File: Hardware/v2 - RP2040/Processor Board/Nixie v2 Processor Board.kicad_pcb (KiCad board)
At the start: 2 copper layers, 100 x 100 mm, 90 parts, among them J1 Conn_02x02_2.54mm, J2 USB_C_Receptacle_USB2.0, J3 Conn_01x03_2.54mm, J4 Conn_01x03_2.54mm, Q1 PZTA92, Q3 MMBTA42, SW1 SW_Push, SW2 SW_Push, SW3 SW_DIP_x10, SW4 SW_Push, U10 W25Q128JVP, U11 L80-M39, U12 DS3231MZ, U13 TC2185-3.3VCTTR, U14 MCP23017_SS, U3 TPS62933, U4 К155ИД1, U5 К155ИД1, U6 К155ИД1, U7 MCP23017_ML, U7 К155ИД1, U8 AP22913, U9 RP2040

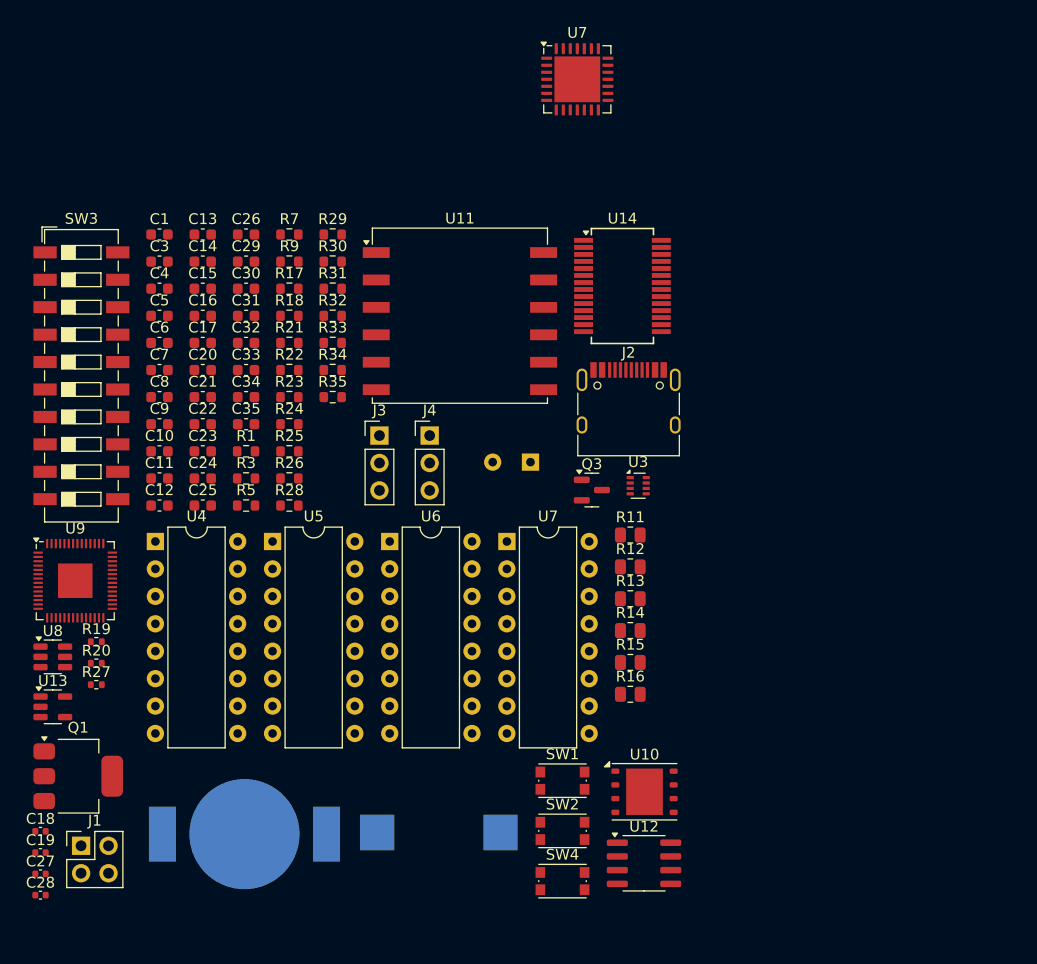
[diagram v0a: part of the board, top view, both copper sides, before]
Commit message: seperated the processor and nixie boards
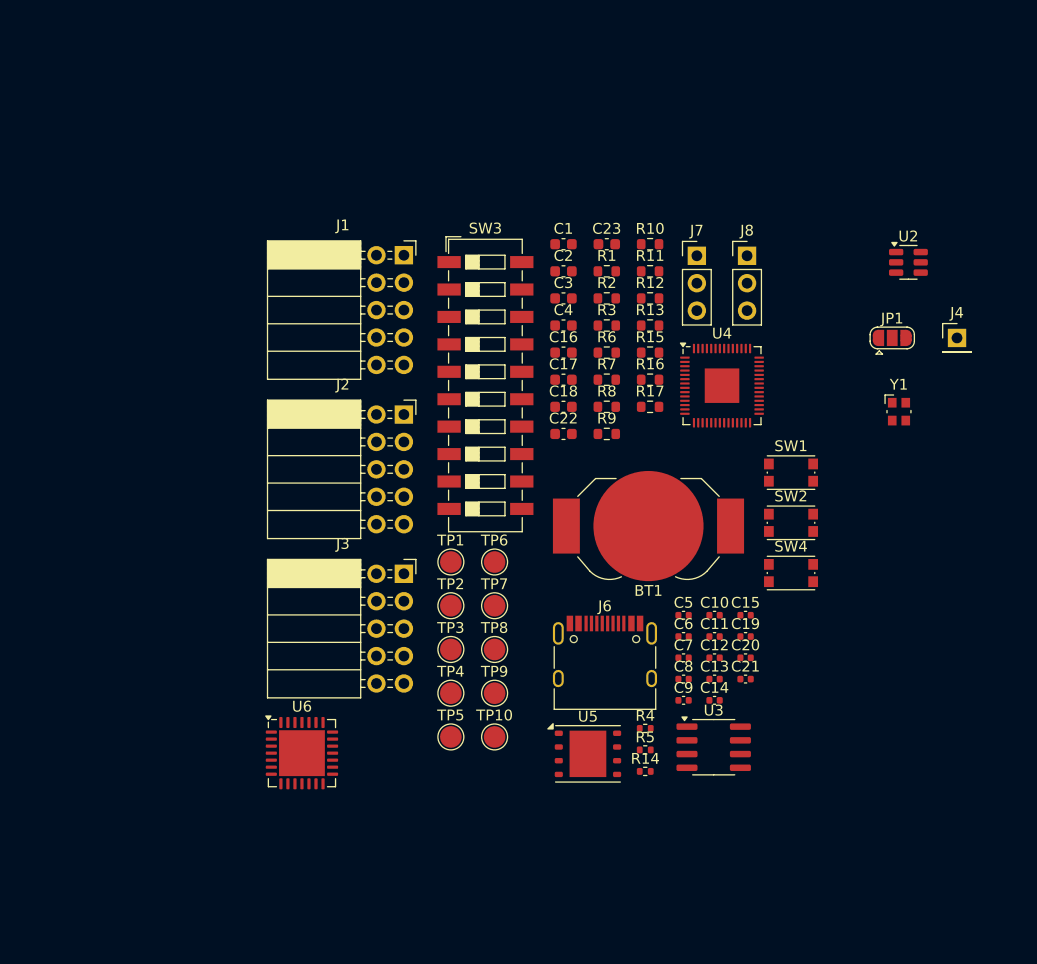
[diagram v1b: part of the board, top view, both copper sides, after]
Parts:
- removed C24, C25, C29, C33, C35: 100n, Capacitor_SMD:C_0603_1608Metric
- removed C26: 10u, Capacitor_SMD:C_0603_1608Metric
- removed C27, C28: 8p, Capacitor_SMD:C_0402_1005Metric
- removed C30, C31, C34: 1u, Capacitor_SMD:C_0603_1608Metric
- removed C32: 10n, Capacitor_SMD:C_0603_1608Metric
- removed L1: 7.8u, Inductor_SMD:L_Vishay_IHLP-5050
- removed Q1: PZTA92, Package_TO_SOT_SMD:SOT-223-3_TabPin2
- removed Q3: MMBTA42, Package_TO_SOT_SMD:SOT-23
- removed R18, R23, R24, R26, R30, R31, R32, R35: 10k, Resistor_SMD:R_0603_1608Metric
- removed R19, R20: 27.4, Resistor_SMD:R_0402_1005Metric
- removed R21, R22: 5.1k, Resistor_SMD:R_0603_1608Metric
- removed R25: 1k, Resistor_SMD:R_0603_1608Metric
- removed R27: 1k, Resistor_SMD:R_0402_1005Metric
- removed R28, R29: 2.2k, Resistor_SMD:R_0603_1608Metric
- removed R33: R_Photo, Resistor_SMD:R_0603_1608Metric
- removed R34: 150, Resistor_SMD:R_0603_1608Metric
- removed U10: W25Q128JVP, Package_SON:WSON-8-1EP_6x5mm_P1.27mm_EP3.4x4.3mm
- removed U11: L80-M39, RF_GPS:Quectel_L80-R
- removed U12: DS3231MZ, Package_SO:SOIC-8_3.9x4.9mm_P1.27mm
- removed U13: TC2185-3.3VCTTR, Package_TO_SOT_SMD:SOT-23-5
- removed U14: MCP23017_SS, Package_SO:SSOP-28_5.3x10.2mm_P0.65mm
- removed U7: MCP23017_ML, Package_DFN_QFN:QFN-28-1EP_6x6mm_P0.65mm_EP4.25x4.25mm
- removed U7: К155ИД1, Package_DIP:DIP-16_W7.62mm
- removed U8: AP22913, Package_TO_SOT_SMD:SOT-23-6
- removed U9: RP2040, Package_DFN_QFN:QFN-56-1EP_7x7mm_P0.4mm_EP3.2x3.2mm
- added J6: USB_C_Receptacle_USB2.0, Connector_USB:USB_C_Receptacle_HRO_TYPE-C-31-M-12, F.Cu at (-36.6, 43.5)
- added J7: Conn_01x03_2.54mm, Connector_PinHeader_2.54mm:PinHeader_1x03_P2.54mm_Vertical, F.Cu at (-28.1, 5.39)
- added J8: Conn_01x03_2.54mm, Connector_PinHeader_2.54mm:PinHeader_1x03_P2.54mm_Vertical, F.Cu at (-23.4, 5.39)
- added JP1: SolderJumper_3_Open, Jumper:SolderJumper-3_P1.3mm_Open_RoundedPad1.0x1.5mm, F.Cu at (-10.0, 13.0)
- added R10: 2.2k, Resistor_SMD:R_0603_1608Metric, F.Cu at (-32.4, 4.32)
- added R2: 169k, Resistor_SMD:R_0603_1608Metric, F.Cu at (-36.4, 9.34)
- added R4: 27.4, Resistor_SMD:R_0402_1005Metric, F.Cu at (-32.9, 49.2)
- added R6: 5.1k, Resistor_SMD:R_0603_1608Metric, F.Cu at (-36.4, 14.4)
- added R8: 10k, Resistor_SMD:R_0603_1608Metric, F.Cu at (-36.4, 19.4)
- added TP1: TestPoint, TestPoint:TestPoint_Pad_D2.0mm, F.Cu at (-50.9, 33.8)
- added TP10: TestPoint, TestPoint:TestPoint_Pad_D2.0mm, F.Cu at (-46.8, 50.0)
- added TP2: TestPoint, TestPoint:TestPoint_Pad_D2.0mm, F.Cu at (-50.9, 37.8)
- added TP3: TestPoint, TestPoint:TestPoint_Pad_D2.0mm, F.Cu at (-50.9, 41.9)
- added TP4: TestPoint, TestPoint:TestPoint_Pad_D2.0mm, F.Cu at (-50.9, 45.9)
- added TP5: TestPoint, TestPoint:TestPoint_Pad_D2.0mm, F.Cu at (-50.9, 50.0)
- added TP6: TestPoint, TestPoint:TestPoint_Pad_D2.0mm, F.Cu at (-46.8, 33.8)
- added TP7: TestPoint, TestPoint:TestPoint_Pad_D2.0mm, F.Cu at (-46.8, 37.8)
- added TP8: TestPoint, TestPoint:TestPoint_Pad_D2.0mm, F.Cu at (-46.8, 41.9)
- added TP9: TestPoint, TestPoint:TestPoint_Pad_D2.0mm, F.Cu at (-46.8, 45.9)
- added U2: AP22913, Package_TO_SOT_SMD:SOT-23-6, F.Cu at (-8.50, 6.00)
- added Y1: 12MHz, Crystal:Crystal_SMD_Abracon_ABM10-4Pin_2.5x2.0mm, F.Cu at (-9.38, 19.8)
- BT1: moved to F.Cu
- C1: value 100u -> 10u
- C10, C11, C12, C13, C5, C9: footprint Capacitor_SMD:C_0603_1608Metric -> Capacitor_SMD:C_0402_1005Metric
- C14, C15: value 100n -> 1u; footprint Capacitor_SMD:C_0603_1608Metric -> Capacitor_SMD:C_0402_1005Metric
- C18: value 1u -> 100n; footprint Capacitor_SMD:C_0402_1005Metric -> Capacitor_SMD:C_0603_1608Metric
- C2: value 4.7u -> 22u; footprint Capacitor_THT:CP_Radial_D8.0mm_P3.50mm -> Capacitor_SMD:C_0603_1608Metric; moved to F.Cu
- C20, C21: value 100n -> 8p; footprint Capacitor_SMD:C_0603_1608Metric -> Capacitor_SMD:C_0402_1005Metric
- C22, C23: value 1u -> 100n
- C3: value 100n -> 1u
- C4: value 10u -> 1u
- C6: value 82p -> 100n; footprint Capacitor_SMD:C_0603_1608Metric -> Capacitor_SMD:C_0402_1005Metric
- C7: value 33n -> 100n; footprint Capacitor_SMD:C_0603_1608Metric -> Capacitor_SMD:C_0402_1005Metric
- C8: value 47u -> 100n; footprint Capacitor_SMD:C_0603_1608Metric -> Capacitor_SMD:C_0402_1005Metric
- J1: value Conn_02x02_2.54mm -> Conn_01x10_Socket; footprint Connector_PinHeader_2.54mm:PinHeader_2x02_P2.54mm_Vertical -> Connector_PinSocket_2.54mm:PinSocket_2x05_P2.54mm_Horizontal
- J2: value USB_C_Receptacle_USB2.0 -> Conn_01x10_Socket; footprint Connector_USB:USB_C_Receptacle_HRO_TYPE-C-31-M-12 -> Connector_PinSocket_2.54mm:PinSocket_2x05_P2.54mm_Horizontal
- J3: value Conn_01x03_2.54mm -> Conn_01x10_Socket; footprint Connector_PinHeader_2.54mm:PinHeader_1x03_P2.54mm_Vertical -> Connector_PinSocket_2.54mm:PinSocket_2x05_P2.54mm_Horizontal
- J4: value Conn_01x03_2.54mm -> Conn_01x01_Pin; footprint Connector_PinHeader_2.54mm:PinHeader_1x03_P2.54mm_Vertical -> Connector_PinHeader_2.54mm:PinHeader_1x01_P2.54mm_Vertical
- R1: value 100k -> 523k
- R11, R15, R16: value 22k -> 10k; footprint Resistor_SMD:R_0805_2012Metric -> Resistor_SMD:R_0603_1608Metric
- R12: value 22k -> 1k; footprint Resistor_SMD:R_0805_2012Metric -> Resistor_SMD:R_0603_1608Metric
- R13: value 220k -> 10k; footprint Resistor_SMD:R_0805_2012Metric -> Resistor_SMD:R_0603_1608Metric
- R14: value 220k -> 1k; footprint Resistor_SMD:R_0805_2012Metric -> Resistor_SMD:R_0402_1005Metric
- R17: value 30.9 -> 10k
- R3: value 100k -> 499k
- R5: value 100k -> 27.4; footprint Resistor_SMD:R_0603_1608Metric -> Resistor_SMD:R_0402_1005Metric
- R7: value 10k -> 5.1k
- R9: value 10k -> 2.2k
- U3: value TPS62933 -> DS3231MZ; footprint Package_TO_SOT_SMD:SOT-583-8 -> Package_SO:SOIC-8_3.9x4.9mm_P1.27mm
- U4: value К155ИД1 -> RP2040; footprint Package_DIP:DIP-16_W7.62mm -> Package_DFN_QFN:QFN-56-1EP_7x7mm_P0.4mm_EP3.2x3.2mm
- U5: value К155ИД1 -> W25Q128JVP; footprint Package_DIP:DIP-16_W7.62mm -> Package_SON:WSON-8-1EP_6x5mm_P1.27mm_EP3.4x4.3mm
- U6: value К155ИД1 -> MCP23017_ML; footprint Package_DIP:DIP-16_W7.62mm -> Package_DFN_QFN:QFN-28-1EP_6x6mm_P0.65mm_EP4.25x4.25mm
- moved C19 68.3 mm to (-23.6, 40.6)
- moved C13 62.8 mm to (-26.5, 44.6)
- moved C14 62.4 mm to (-26.5, 46.6)
- moved C18 62.4 mm to (-40.4, 19.4)
- moved J1 62.3 mm to (-55.2, 5.34)
- moved C15 58.7 mm to (-23.6, 38.7)
- moved C20 56.9 mm to (-23.6, 42.6)
- moved C21 56.6 mm to (-23.6, 44.6)
- moved C5 55.9 mm to (-29.3, 38.7)
- moved C6 55.6 mm to (-29.3, 40.6)
- moved C7 55.4 mm to (-29.3, 42.6)
- moved C8 55.1 mm to (-29.3, 44.6)
- moved C9 54.9 mm to (-29.3, 46.6)
- moved U4 54.4 mm to (-25.8, 17.4)
- moved C10 53.6 mm to (-26.5, 38.7)
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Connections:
- C10 pad 1: +1V1 -> +3.3V
- C14 pad 1: +3.3V -> +1V1
- C16 pad 1: +3.3V -> Net-(U4-RUN)
- C17 pad 1: +3.3V -> +3V3
- C18 pad 1: +1V1 -> Net-(C18-Pad1)
- C19 pad 1: +3.3V -> Net-(BT1-+)
- C2 pad 1: /170V_1 -> +3.3V
- C20 pad 1: Net-(U9-RUN) -> GND
- C20 pad 2: GND -> Net-(U4-XIN)
- C21 pad 1: Net-(C21-Pad1) -> GND
- C21 pad 2: GND -> Net-(C21-Pad2)
- C23 pad 1: Net-(U11-VCC) -> Net-(U6-GPA2)
- C3 pad 1: Net-(U3-BST) -> Net-(JP1-C)
- C3 pad 2: Net-(U3-SW) -> GND
- C4 pad 1: VBUS -> Net-(U2-OUT)
- C5 pad 1: VBUS -> +1V1
- C6 pad 1: +3.3V -> +1V1
- C6 pad 2: Net-(U3-FB) -> GND
- C7 pad 1: Net-(U3-SS) -> +3.3V
- C9 pad 1: +1V1 -> +3.3V
- J1 pad 2: Net-(J1-Pin_2) -> /Hours_Tens_A
- J1 pad 3: GND -> /Hours_Tens_D
- J1 pad 4: Net-(J1-Pin_4) -> /Hours_Tens_B
- J3 pad 1: GND -> VBUS
- J3 pad 2: /UART0 RX -> VBUS
- J3 pad 3: /UART0 TX -> +3.3V
- J4 pad 1: Net-(J4-Pin_1) -> /UART1_TX
- R1 pad 1: /170V_1 -> Net-(U1-FB)
- R1 pad 2: Net-(Q1-B) -> +3.3V
- R11 pad 1: /ANODE_1 -> Net-(C18-Pad1)
- R11 pad 2: Net-(N1-Anode) -> +3.3V
- R12 pad 1: /ANODE_1 -> Net-(U4-QSPI_SS)
- R12 pad 2: Net-(N2-Anode) -> Net-(C18-Pad1)
- R13 pad 1: /ANODE_1 -> +3V3
- R13 pad 2: Net-(J1-Pin_2) -> /RTC_Interrupt
- R14 pad 1: /ANODE_1 -> Net-(U4-XOUT)
- R14 pad 2: Net-(J1-Pin_4) -> Net-(C21-Pad2)
- R15 pad 1: /ANODE_1 -> +3V3
- R15 pad 2: Net-(N3-Anode) -> Net-(U6-~{RESET})
- R16 pad 1: /ANODE_1 -> +3V3
- R16 pad 2: Net-(N4-Anode) -> /Settings_Interrupt
- R17 pad 1: Net-(U3-FB) -> +3V3
- R17 pad 2: +3.3V -> Net-(U6-INTB)
- R3 pad 1: Net-(Q1-B) -> Net-(U1-PG)
- R3 pad 2: Net-(R3-Pad2) -> +3.3V
- R5 pad 1: Net-(R3-Pad2) -> Net-(U4-USB_DP)
- R7 pad 1: /Dimming -> GND
- R9 pad 1: /Dimming -> +3V3
- R9 pad 2: GND -> /I2C1_SCL
- SW1 pad 2: Net-(U9-RUN) -> Net-(U4-RUN)
- SW2 pad 2: Net-(C21-Pad1) -> Net-(C18-Pad1)
- SW3 pad 1: Net-(U7-GPB0) -> Net-(U6-GPB0)
- SW3 pad 10: Net-(U7-GPA1) -> Net-(U6-GPA1)
- SW3 pad 2: Net-(U7-GPB1) -> Net-(U6-GPB1)
- SW3 pad 3: Net-(U7-GPB2) -> Net-(U6-GPB2)
- SW3 pad 4: Net-(U7-GPB3) -> Net-(U6-GPB3)
- SW3 pad 5: Net-(U7-GPB4) -> Net-(U6-GPB4)
- SW3 pad 6: Net-(U7-GPB5) -> Net-(U6-GPB5)
- SW3 pad 7: Net-(U7-GPB6) -> Net-(U6-GPB6)
- SW3 pad 8: Net-(U7-GPB7) -> Net-(U6-GPB7)
- SW3 pad 9: Net-(U7-GPA0) -> Net-(U6-GPA0)
- SW4 pad 1: Net-(U7-GPA2) -> Net-(U6-GPA2)
- U3 pad 2: unconnected-(U3-EN-Pad2) -> +3V3
- U3 pad 3: VBUS -> /RTC_Interrupt
- U3 pad 4: GND -> +3V3
- U3 pad 5: Net-(U3-SW) -> GND
- U3 pad 6: Net-(U3-BST) -> Net-(BT1-+)
- U3 pad 7: Net-(U3-SS) -> /I2C1_SDA
- U3 pad 8: Net-(U3-FB) -> /I2C1_SCL
- U4 pad 1: Net-(U4-8) -> +3.3V
- U4 pad 10: Net-(U4-7) -> +3.3V
- U4 pad 11: Net-(U4-6) -> /Hours_Tens_B
- U4 pad 12: GND -> /Hours_Tens_C
- U4 pad 13: Net-(U4-4) -> /Hours_Ones_A
- U4 pad 14: Net-(U4-5) -> /Hours_Ones_D
- U4 pad 15: Net-(U4-1) -> /Hours_Ones_B
- U4 pad 16: Net-(N1-0) -> /Hours_Ones_C
- U4 pad 2: Net-(U4-9) -> /UART0 TX
- U4 pad 3: /Hours_Tens_A -> /UART0 RX
- U4 pad 4: /Hours_Tens_D -> /I2C1_SDA
- U4 pad 5: VBUS -> /I2C1_SCL
- U4 pad 6: /Hours_Tens_B -> /UART1_TX
- U4 pad 7: /Hours_Tens_C -> /UART1_RX
- U4 pad 8: Net-(U4-2) -> /Hours_Tens_A
- U4 pad 9: Net-(U4-3) -> /Hours_Tens_D
- U5 pad 1: Net-(U5-8) -> Net-(U4-QSPI_SS)
- U5 pad 2: Net-(U5-9) -> Net-(U4-QSPI_SD1)
- U5 pad 3: /Hours_Ones_A -> Net-(U4-QSPI_SD2)
- U5 pad 4: /Hours_Ones_D -> GND
- U5 pad 5: VBUS -> Net-(U4-QSPI_SD0)
- U5 pad 6: /Hours_Ones_B -> Net-(U4-QSPI_SCLK)
- U5 pad 7: /Hours_Ones_C -> Net-(U4-QSPI_SD3)
- U5 pad 8: Net-(U5-2) -> +3V3
- U5 pad 9: Net-(U5-3) -> GND
- U6 pad 1: Net-(U6-8) -> Net-(U6-GPB4)
- U6 pad 10: Net-(U6-7) -> unconnected-(U6-NC-Pad10)
- U6 pad 11: Net-(U6-6) -> GND
- U6 pad 13: Net-(U6-4) -> GND
- U6 pad 14: Net-(U6-5) -> Net-(U6-~{RESET})
- U6 pad 15: Net-(U6-1) -> Net-(U6-INTB)
- U6 pad 16: Net-(N3-0) -> /Settings_Interrupt
- U6 pad 2: Net-(U6-9) -> Net-(U6-GPB5)
- U6 pad 3: /Mins_Tens_A -> Net-(U6-GPB6)
- U6 pad 4: /Mins_Tens_D -> Net-(U6-GPB7)
- U6 pad 5: VBUS -> +3V3
- U6 pad 6: /Mins_Tens_B -> GND
- U6 pad 7: /Mins_Tens_C -> unconnected-(U6-NC-Pad7)
- U6 pad 8: Net-(U6-2) -> /I2C1_SCL
- U6 pad 9: Net-(U6-3) -> /I2C1_SDA

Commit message: Started board layout
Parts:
- added H1: MountingHole_Pad, MountingHole:MountingHole_3.2mm_M3_Pad_Via, F.Cu at (105.0, 55.0)
- added H2: MountingHole_Pad, MountingHole:MountingHole_3.2mm_M3_Pad_Via, F.Cu at (195.0, 55.0)
- added H3: MountingHole_Pad, MountingHole:MountingHole_3.2mm_M3_Pad_Via, F.Cu at (105.0, 95.0)
- added H4: MountingHole_Pad, MountingHole:MountingHole_3.2mm_M3_Pad_Via, F.Cu at (195.0, 95.0)
- added J5: AudioJack3_SwitchT, Connector_Audio:Jack_3.5mm_CUI_SJ-3524-SMT_Horizontal, F.Cu at (114.5, 58.7)
- added U1: TPS82084SIL, Nick_Converter_DCDC:MicroSiP 1.33mm, F.Cu at (125.6, 66.4)
- BT1: moved to B.Cu
- C19: footprint Capacitor_SMD:C_0402_1005Metric -> Capacitor_SMD:C_0603_1608Metric
- JP1: footprint Jumper:SolderJumper-3_P1.3mm_Open_RoundedPad1.0x1.5mm -> Jumper:SolderJumper-3_P1.3mm_Open_RoundedPad1.0x1.5mm_NumberLabels
- SW3: footprint Button_Switch_SMD:SW_DIP_SPSTx10_Slide_6.7x26.96mm_W6.73mm_P2.54mm_LowProfile_JPin -> Button_Switch_THT:SW_DIP_SPSTx10_Piano_10.8x26.96mm_W7.62mm_P2.54mm
- moved TP10 243.0 mm to (195.0, 74.0)
- moved TP9 243.0 mm to (195.0, 70.0)
- moved U6 242.6 mm to (177.1, 71.5), turned to 45 degrees
- moved TP6 240.3 mm to (191.0, 68.0)
- moved TP7 240.3 mm to (191.0, 72.0)
- moved TP8 240.3 mm to (191.0, 76.1)
- moved J3 239.9 mm to (178.9, 87.4), turned to 90 degrees
- moved SW3 239.0 mm to (188.4, 54.2), turned to -90 degrees
- moved BT1 229.7 mm to (193.0, 74.0), turned to -90 degrees
- moved U3 193.1 mm to (165.3, 73.3)
- moved U5 186.0 mm to (147.5, 62.5)
- moved SW4 179.4 mm to (159.0, 54.0), turned to 90 degrees
- moved R7 175.0 mm to (132.6, 62.2), turned to 90 degrees
- moved R6 164.6 mm to (121.2, 61.8), turned to 90 degrees
- moved J4 164.1 mm to (-120.5, 128.5)
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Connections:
- C23 pad 1: Net-(U6-GPA2) -> Net-(U6-GPB2)
- J1 pad 1: GND -> /Hours_Ones_B
- J1 pad 10: GND -> /Hours_Tens_A
- J1 pad 2: /Hours_Tens_A -> /Hours_Ones_C
- J1 pad 3: /Hours_Tens_D -> /Hours_Ones_A
- J1 pad 4: /Hours_Tens_B -> /Hours_Ones_D
- J1 pad 5: /Hours_Tens_C -> GND
- J1 pad 6: /Hours_Ones_C -> GND
- J1 pad 7: /Hours_Ones_B -> /Hours_Tens_C
- J1 pad 8: /Hours_Ones_D -> /Hours_Tens_B
- J1 pad 9: /Hours_Ones_A -> /Hours_Tens_D
- J2 pad 1: GND -> /Minutes_Ones_B
- J2 pad 10: GND -> /Minutes_Tens_A
- J2 pad 2: /Minutes_Tens_A -> /Minutes_Ones_C
- J2 pad 3: /Minutes_Tens_D -> /Minutes_Ones_A
- J2 pad 4: /Minutes_Tens_B -> /Minutes_Ones_D
- J2 pad 5: /Minutes_Tens_C -> GND
- J2 pad 6: /Minutes_Ones_C -> GND
- J2 pad 7: /Minutes_Ones_B -> /Minutes_Tens_C
- J2 pad 8: /Minutes_Ones_D -> /Minutes_Tens_B
- J2 pad 9: /Minutes_Ones_A -> /Minutes_Tens_D
- SW3 pad 1: Net-(U6-GPB0) -> GND
- SW3 pad 10: Net-(U6-GPA1) -> GND
- SW3 pad 11: GND -> Net-(U6-GPB1)
- SW3 pad 12: GND -> Net-(U6-GPB0)
- SW3 pad 13: GND -> Net-(U6-GPA7)
- SW3 pad 14: GND -> Net-(U6-GPA6)
- SW3 pad 15: GND -> Net-(U6-GPA5)
- SW3 pad 16: GND -> Net-(U6-GPA4)
- SW3 pad 17: GND -> Net-(U6-GPA3)
- SW3 pad 18: GND -> Net-(U6-GPA2)
- SW3 pad 19: GND -> Net-(U6-GPA1)
- SW3 pad 2: Net-(U6-GPB1) -> GND
- SW3 pad 20: GND -> Net-(U6-GPA0)
- SW3 pad 3: Net-(U6-GPB2) -> GND
- SW3 pad 4: Net-(U6-GPB3) -> GND
- SW3 pad 5: Net-(U6-GPB4) -> GND
- SW3 pad 6: Net-(U6-GPB5) -> GND
- SW3 pad 7: Net-(U6-GPB6) -> GND
- SW3 pad 8: Net-(U6-GPB7) -> GND
- SW3 pad 9: Net-(U6-GPA0) -> GND
- SW4 pad 1: Net-(U6-GPA2) -> Net-(U6-GPB2)
- TP10 pad 1: Net-(U6-GPA7) -> Net-(U6-GPB7)
- TP6 pad 1: Net-(U6-GPA3) -> Net-(U6-GPB3)
- TP7 pad 1: Net-(U6-GPA4) -> Net-(U6-GPB4)
- TP8 pad 1: Net-(U6-GPA5) -> Net-(U6-GPB5)
- TP9 pad 1: Net-(U6-GPA6) -> Net-(U6-GPB6)
- U4 pad 11: /Hours_Tens_B -> /Hours_Ones_A
- U4 pad 12: /Hours_Tens_C -> /Hours_Ones_D
- U4 pad 13: /Hours_Ones_A -> /Hours_Tens_C
- U4 pad 14: /Hours_Ones_D -> /Hours_Tens_B
- U4 pad 15: /Hours_Ones_B -> /Hours_Tens_D
- U4 pad 16: /Hours_Ones_C -> /Hours_Tens_A
- U4 pad 17: /Minutes_Tens_A -> /Minutes_Ones_C
- U4 pad 18: /Minutes_Tens_D -> /Minutes_Ones_B
- U4 pad 27: /Minutes_Tens_B -> /Minutes_Ones_A
- U4 pad 28: /Minutes_Tens_C -> /Minutes_Ones_D
- U4 pad 29: /Minutes_Ones_A -> /Minutes_Tens_B
- U4 pad 30: /Minutes_Ones_D -> /Minutes_Tens_C
- U4 pad 31: /Minutes_Ones_B -> /Minutes_Tens_D
- U4 pad 32: /Minutes_Ones_C -> /Minutes_Tens_A
- U4 pad 8: /Hours_Tens_A -> /Hours_Ones_B
- U4 pad 9: /Hours_Tens_D -> /Hours_Ones_C
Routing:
- net Net-(U6-GPA4): track 0.00 -> 0.79 mm
- net Net-(U6-GPB0): track 0.00 -> 0.68 mm
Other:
- board size 100 x 100 mm -> 100 x 50 mm
- board text added: "DCDC"
- board text added: "GPS"
- board text added: "INTERCONNECT"
- board text added: "RP2040"
- board text added: "RTC"
- board text added: "SETTINGS"
- board text added: "USB"

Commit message: Laied out indivdual circuit blocks
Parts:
- moved TP1 343.7 mm to (193.0, 87.9), turned to 180 degrees
- moved TP2 342.2 mm to (193.0, 83.8), turned to 180 degrees
- moved U3 297.9 mm to (-132.1, 56.1)
- moved TP10 265.3 mm to (-62.5, 138.2)
- moved TP6 265.3 mm to (-66.5, 132.2)
- moved TP7 265.3 mm to (-66.5, 136.2)
- moved TP8 265.3 mm to (-66.5, 140.3)
- moved TP9 265.3 mm to (-62.5, 134.2)
- moved U1 258.2 mm to (-131.3, 92.1), turned to -90 degrees
- moved J4 249.8 mm to (122.0, 68.5)
- moved U6 246.1 mm to (-65.3, 114.4), turned to 0 degrees
- moved U2 242.2 mm to (-128.7, 125.8)
- moved JP1 240.4 mm to (-128.9, 131.2), turned to 180 degrees
- moved C23 234.3 mm to (159.0, 57.8)
- moved C18 215.3 mm to (140.0, 57.9), turned to 180 degrees
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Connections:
- net Net-(J6-D+-PadA6) renamed /USB_D+
- net Net-(J6-D--PadA7) renamed /USB_D-
- net Net-(U4-USB_DM) renamed /USB_RP_D-
- net Net-(U4-USB_DP) renamed /USB_RP_D+
- C10 pad 1: +3.3V -> +3V3
- C11 pad 1: +3.3V -> +3V3
- C12 pad 1: +3.3V -> +3V3
- C13 pad 1: +3.3V -> +3V3
- C15 pad 1: +3.3V -> +3V3
- C2 pad 1: +3.3V -> +3V3
- C7 pad 1: +3.3V -> +3V3
- C8 pad 1: +3.3V -> +3V3
- C9 pad 1: +3.3V -> +3V3
- J3 pad 3: +3.3V -> +3V3
- JP1 pad 3: +3.3V -> +3V3
- R1 pad 2: +3.3V -> +3V3
- R11 pad 2: +3.3V -> +3V3
- R3 pad 2: +3.3V -> +3V3
- R8 pad 2: +3.3V -> +3V3
- U1 pad 8: +3.3V -> +3V3
- U4 pad 1: +3.3V -> +3V3
- U4 pad 10: +3.3V -> +3V3
- U4 pad 22: +3.3V -> +3V3
- U4 pad 33: +3.3V -> +3V3
- U4 pad 42: +3.3V -> +3V3
- U4 pad 43: +3.3V -> +3V3
- U4 pad 44: +3.3V -> +3V3
- U4 pad 48: +3.3V -> +3V3
- U4 pad 49: +3.3V -> +3V3
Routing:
- net +3V3: track 0.00 -> 37.8 mm, vias 0 -> 7
- net +1V1: track 0.00 -> 27.8 mm, vias 0 -> 3
- net Net-(U4-QSPI_SD3): track 0.00 -> 16.9 mm
- net Net-(U4-QSPI_SCLK): track 0.00 -> 15.0 mm
- net Net-(U4-QSPI_SD0): track 0.00 -> 13.1 mm
- net Net-(U4-XIN): track 0.00 -> 12.6 mm
- net Net-(JP1-C): track 0.00 -> 11.3 mm
- net Net-(U4-QSPI_SS): track 0.00 -> 10.3 mm
- net VBUS: track 0.00 -> 8.18 mm, vias 0 -> 2
- net Net-(U4-QSPI_SD1): track 0.00 -> 7.81 mm
- net /I2C1_SDA: track 0.00 -> 7.75 mm
- net /I2C1_SCL: track 0.00 -> 7.74 mm
- net Net-(U4-QSPI_SD2): track 0.00 -> 7.04 mm
- net GND: track 0.00 -> 6.93 mm, vias 0 -> 8
- net /Minutes_Ones_B: track 0.00 -> 6.68 mm
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- added copper zone on B.Cu, net +3V3
- added copper zone on F.Cu, net +3V3
- added copper zone on B.Cu, net GND
- added copper zone on F.Cu, net GND

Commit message: Started placing assembled blocks on the board and routing
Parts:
- moved C19 307.2 mm to (180.1, 81.0)
- moved C17 307.2 mm to (168.4, 78.0)
- moved R13 307.2 mm to (168.4, 81.1)
- moved U3 307.2 mm to (174.2, 79.5)
- moved R2 284.6 mm to (152.0, 66.2), turned to 90 degrees
- moved R1 281.4 mm to (150.4, 64.5), turned to 90 degrees
- moved U1 280.2 mm to (147.7, 66.5), turned to 0 degrees
- moved C2 278.0 mm to (148.0, 63.7), turned to 180 degrees
- moved C1 277.5 mm to (145.1, 66.7), turned to 90 degrees
- moved R3 276.6 mm to (148.0, 62.1), turned to 0 degrees
- moved C4 242.2 mm to (105.7, 66.3)
- moved JP1 242.2 mm to (105.2, 68.9)
- moved C3 242.2 mm to (105.0, 60.8)
- moved U2 242.2 mm to (105.4, 63.5)
- moved C22 237.0 mm to (161.4, 69.2)
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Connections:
- net Net-(U4-QSPI_SS) renamed /BOOT_SEL
- net Net-(U4-RUN) renamed /RESET
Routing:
- net /UART1_RX: track 2.39 -> 39.2 mm
- net /USB_D+: track 0.00 -> 28.2 mm
- net /Minutes_Ones_B: track 6.68 -> 34.7 mm
- net VBUS: track 8.18 -> 36.0 mm, vias 2 -> 5
- net /USB_D-: track 0.00 -> 27.0 mm
- net /Minutes_Ones_C: track 6.19 -> 33.1 mm
- net /Hours_Ones_C: track 2.50 -> 26.5 mm
- net /UART1_TX: track 2.34 -> 25.8 mm
- net /Hours_Ones_B: track 2.41 -> 24.9 mm
- net Net-(U6-GPA0): track 0.27 -> 21.6 mm
- net /Hours_Ones_D: track 2.55 -> 22.4 mm
- net /Minutes_Tens_A: track 2.90 -> 22.7 mm
- net Net-(U6-GPA1): track 0.00 -> 18.9 mm
- net Net-(U6-GPB2): track 0.02 -> 18.5 mm
- net /Hours_Ones_A: track 2.66 -> 20.6 mm
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
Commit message: started nixie layout, added bleed resistor to HV cap
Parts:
- J1, J2, J3: footprint Connector_PinSocket_2.54mm:PinSocket_2x05_P2.54mm_Horizontal -> Connector_PinSocket_2.54mm:PinSocket_2x05_P2.54mm_Vertical
- moved TP10 266.3 mm to (179.7, 34.1)
- moved TP6 266.3 mm to (175.7, 28.0)
- moved TP7 266.3 mm to (175.7, 32.1)
- moved TP8 266.3 mm to (175.7, 36.1)
- moved TP9 266.3 mm to (179.7, 30.0)
- moved TP4 209.4 mm to (148.8, 118.7)
- moved TP3 209.4 mm to (152.0, 121.2)
- moved TP5 209.4 mm to (152.0, 116.2)
- moved C19 77.1 mm to (113.3, 119.5)
- moved C17 77.1 mm to (101.6, 116.6)
- moved R13 77.1 mm to (101.6, 119.6)
- moved U3 77.1 mm to (107.4, 118.1)
- moved BT1 50.6 mm to (188.3, 124.4)
- moved TP2 27.2 mm to (177.9, 106.5)
- moved TP1 27.2 mm to (177.9, 110.6)
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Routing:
- net /Minutes_Ones_B: track 34.7 -> 29.5 mm
- net /Minutes_Ones_C: track 33.1 -> 28.0 mm
- net Net-(U4-XIN): track 12.6 -> 10.7 mm
- net Net-(U4-XOUT): track 6.18 -> 4.71 mm
- net GND: vias 8 -> 9
